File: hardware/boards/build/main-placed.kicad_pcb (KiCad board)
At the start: 4 copper layers, 140 x 84 mm, 151 parts

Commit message: Parts audit complete
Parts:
- removed the REF** at (24.2, 14.8)
- removed the REF** at (40.8, 35.9)
- removed the REF** at (105.9, 14.8)
- removed the REF** at (136.6, 62.5)
- removed the REF** at (111.2, 20.6)
- removed the REF** at (111.0, 14.8)
- removed the REF** at (73.9, 62.6)
- removed the REF** at (91.6, 26.4)
- removed the REF** at (102.9, 30.9)
- removed the REF** at (50.0, 53.3)
- removed the REF** at (18.6, 14.8)
- removed the REF** at (83.8, 62.6)
- removed the REF** at (50.0, 41.0)
- removed the REF** at (111.2, 61.8)
- removed the REF** at (18.6, 9.70)
- removed the REF** at (89.0, 14.8)
- added REF**: SOT-23, BAT54S:SOT-23, F.Cu at (136.6, 25.9)
- added REF**: TSSOP-14, OPA4171AIPWR:TSSOP-14, F.Cu at (107.2, 65.9)
- added REF**: WQFN-16, DAC80508ZRTER:WQFN-16, F.Cu at (49.8, 52.9)
- added REF**: SOD-123, B5819W:SOD-123, F.Cu at (40.6, 35.7)
- added REF**: SOT-23, BAT54S:SOT-23, F.Cu at (136.6, 20.6)
- added REF**: SOD-123, B5819W:SOD-123, F.Cu at (24.1, 14.7)
- added REF**: SOT-23, BAT54S:SOT-23, F.Cu at (110.8, 73.6)
- added REF**: TSSOP-14, OPA4171AIPWR:TSSOP-14, F.Cu at (75.4, 62.6)
- added REF**: TSSOP-14, OPA4171AIPWR:TSSOP-14, F.Cu at (85.8, 62.6)
- added REF**: SOD-123, B5819W:SOD-123, F.Cu at (18.5, 14.7)
- added REF**: TSSOP-14, OPA4171AIPWR:TSSOP-14, F.Cu at (85.5, 73.6)
- added REF**: WQFN-16, DAC80508ZRTER:WQFN-16, F.Cu at (49.8, 40.8)
- added REF**: TSSOP-14, OPA4171AIPWR:TSSOP-14, F.Cu at (107.7, 55.3)
- added REF**: SOT-23, BAT54S:SOT-23, F.Cu at (105.7, 30.6)
- added REF**: SOD-123, B5819W:SOD-123, F.Cu at (18.5, 9.60)
- added REF**: SOT-23, BAT54S:SOT-23, F.Cu at (110.7, 25.6)
- moved C29 83.8 mm to (114.8, 14.7)
- moved C24 83.8 mm to (109.8, 9.60)
- moved R31 79.3 mm to (104.7, 9.60)
- moved R1 79.3 mm to (99.6, 4.53)
- moved R32 74.9 mm to (94.6, 4.53)
- moved C14 74.3 mm to (84.4, 4.53)
- moved C18 72.0 mm to (79.3, 9.60)
- moved C31 70.3 mm to (94.6, 9.60)
- moved C22 69.2 mm to (99.6, 9.60)
- moved R66 69.1 mm to (70.3, 78.6)
- moved C8 67.7 mm to (105.7, 20.5)
- moved C20 67.5 mm to (89.5, 9.60)
- moved C26 66.7 mm to (94.6, 14.7)
- moved C21 66.7 mm to (99.6, 14.7)
- moved C19 66.4 mm to (89.5, 4.53)
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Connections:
- R10 pad 1: 6 -> 9
- R11 pad 1: dac-7-2 -> dac-7-1
- R13 pad 1: 7 -> dac-10
- R16 pad 1: 8 -> 11
- R23 pad 1: dac-7 -> 7
- R37 pad 1: dac-7-1 -> dac-7
- R39 pad 1: dac-7-1 -> dac-7
- R61 pad 1: 5-1 -> 3
- R62 pad 1: 6-1 -> 11-1
- R7 pad 1: 5 -> 8
- R75 pad 2: 3 -> DP
- R9 pad 1: dac-7-2 -> dac-7-1
- REF** pad 1: VBUS -> hv
- REF** pad 2: hv -> VBUS
- REF** pad 4: DM -> DP
- REF** pad 5: 5-1 -> DM
- REF** pad 6: 6-1 -> 6
- REF** pad 7: hv -> VBUS
- REF** pad 2: c_filter-power-hv-4 -> c_vio2-power-hv
- REF** pad 3: c_vio2-power-hv -> c_filter-power-hv-3
- REF** pad 1: BASE -> hv
- REF** pad 2: hv -> BASE-1
- REF** pad 3: COLLECTOR -> COLLECTOR-1
- REF** pad 23: i2c_sda -> 23
- REF** pad 24: i2c_scl -> i2c_sda
- REF** pad 25: 25 -> i2c_scl
- REF** pad 1: BASE-1 -> hv
- REF** pad 2: hv -> BASE
- REF** pad 3: COLLECTOR-1 -> COLLECTOR
- REF** pad 3: 3 -> DP

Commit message: Fix firmware
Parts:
- removed the REF** at (136.6, 25.9)
- removed the REF** at (107.2, 65.9)
- removed the REF** at (49.8, 52.9)
- removed the REF** at (136.6, 57.3)
- removed the REF** at (40.6, 35.7)
- removed the REF** at (136.6, 20.6)
- removed the REF** at (24.1, 14.7)
- removed the REF** at (110.8, 73.6)
- removed the REF** at (75.4, 62.6)
- removed the REF** at (85.8, 62.6)
- removed the REF** at (18.5, 14.7)
- removed the REF** at (85.5, 73.6)
- removed the REF** at (49.8, 40.8)
- removed the REF** at (107.7, 55.3)
- removed the REF** at (105.7, 30.6)
- removed the REF** at (18.5, 9.60)
- removed the REF** at (110.7, 25.6)
- added R76: 27Ω, UNI_ROYAL_0402WGF270JTCE:R0402, F.Cu at (30.5, 55.5)
- added R77: 27Ω, UNI_ROYAL_0402WGF270JTCE:R0402, F.Cu at (30.5, 50.5)
- added REF**: WQFN-16, DAC80508ZRTER:WQFN-16, F.Cu at (70.2, 62.6)
- added REF**: SOT-23, BAT54S:SOT-23, F.Cu at (133.6, 4.50)
- added REF**: SOT-23, BAT54S:SOT-23, F.Cu at (129.5, 78.5)
- added REF**: TSSOP-14, OPA4171AIPWR:TSSOP-14, F.Cu at (88.5, 61.9)
- added REF**: SOT-23, BAT54S:SOT-23, F.Cu at (114.5, 78.5)
- added REF**: TSSOP-14, OPA4171AIPWR:TSSOP-14, F.Cu at (94.5, 68.5)
- added REF**: SOT-23, BAT54S:SOT-23, F.Cu at (128.6, 4.50)
- added REF**: SOT-23, BAT54S:SOT-23, F.Cu at (128.6, 14.5)
- added REF**: SOT-23, BAT54S:SOT-23, F.Cu at (113.5, 4.50)
- added REF**: SOD-123, B5819W:SOD-123, F.Cu at (30.5, 30.5)
- added REF**: WQFN-16, DAC80508ZRTER:WQFN-16, F.Cu at (50.0, 50.5)
- added REF**: TSSOP-14, OPA4171AIPWR:TSSOP-14, F.Cu at (112.2, 67.9)
- added REF**: TSSOP-14, OPA4171AIPWR:TSSOP-14, F.Cu at (92.0, 31.2)
- added REF**: SOD-123, B5819W:SOD-123, F.Cu at (24.0, 14.5)
- added REF**: SOD-123, B5819W:SOD-123, F.Cu at (18.5, 14.5)
- added REF**: TSSOP-14, OPA4171AIPWR:TSSOP-14, F.Cu at (78.6, 62.6)
- added REF**: SOD-123, B5819W:SOD-123, F.Cu at (18.5, 9.50)
- R34, R37, R40, R43: value 6.04kΩ -> 10kΩ; footprint UNI_ROYAL_0402WGF6041TCE:R0402 -> UNI_ROYAL_0603WAF1002T5E:R0603
- R36, R39, R42, R45: value 470Ω -> 6.04kΩ; footprint UNI_ROYAL_0603WAF4700T5E:R0603 -> UNI_ROYAL_0402WGF6041TCE:R0402
- R38, R41, R44, R47: value 10kΩ -> 470Ω; footprint UNI_ROYAL_0603WAF1002T5E:R0603 -> UNI_ROYAL_0603WAF4700T5E:R0603
- R46: value 200Ω -> 10kΩ; footprint UNI_ROYAL_0603WAF2000T5E:R0603 -> UNI_ROYAL_0603WAF1002T5E:R0603
- R48: value 10kΩ -> 200Ω; footprint UNI_ROYAL_0603WAF1002T5E:R0603 -> UNI_ROYAL_0603WAF2000T5E:R0603
- R50: value 22kΩ -> 10kΩ; footprint UNI_ROYAL_0603WAF2202T5E:R0603 -> UNI_ROYAL_0603WAF1002T5E:R0603
- R61: value 5.1kΩ -> 10kΩ; footprint UNI_ROYAL_0402WGF5101TCE:R0402 -> UNI_ROYAL_0603WAF1002T5E:R0603
- R62: value 5.1kΩ -> 22kΩ; footprint UNI_ROYAL_0402WGF5101TCE:R0402 -> UNI_ROYAL_0603WAF2202T5E:R0603
- R63, R64: value 1kΩ -> 5.1kΩ; footprint UNI_ROYAL_0603WAF1001T5E:R0603 -> UNI_ROYAL_0402WGF5101TCE:R0402
- R65, R66, R73: value 10kΩ -> 1kΩ; footprint UNI_ROYAL_0603WAF1002T5E:R0603 -> UNI_ROYAL_0603WAF1001T5E:R0603
- R71, R72: value 1kΩ -> 10kΩ; footprint UNI_ROYAL_0603WAF1001T5E:R0603 -> UNI_ROYAL_0603WAF1002T5E:R0603
- R74: value 27Ω -> 1kΩ; footprint UNI_ROYAL_0402WGF270JTCE:R0402 -> UNI_ROYAL_0603WAF1001T5E:R0603
- R75: value 27Ω -> 10kΩ; footprint UNI_ROYAL_0402WGF270JTCE:R0402 -> UNI_ROYAL_0603WAF1002T5E:R0603
- moved R64 132.8 mm to (4.58, 37.9)
- moved R62 125.1 mm to (124.5, 73.5)
- moved R74 107.1 mm to (136.6, 36.3)
- moved R55 101.5 mm to (53.5, 9.50)
- moved R50 96.1 mm to (40.5, 35.5)
- moved R63 95.9 mm to (9.75, 37.9)
- moved R49 93.1 mm to (35.5, 40.5)
- moved C29 92.6 mm to (39.5, 68.5)
- moved C24 91.3 mm to (44.5, 73.5)
- moved R59 86.7 mm to (63.5, 4.50)
- moved R57 84.2 mm to (49.5, 73.5)
- moved C47 82.8 mm to (54.5, 73.5)
- moved R66 81.6 mm to (136.6, 31.1)
- moved R32 81.5 mm to (40.5, 65.5)
- moved R31 81.4 mm to (45.5, 65.5)
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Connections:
- R34 pad 1: dac-1 -> c_vio2-power-hv
- R34 pad 2: dac-IN1_N-1 -> SDO
- R35 pad 1: dac-IN1_N-1 -> c_vio2-power-hv
- R35 pad 2: hv -> dac-SDO
- R36 pad 2: vel1 -> dac-IN1_N-1
- R37 pad 1: dac-7 -> dac-IN1_N-1
- R37 pad 2: dac-IN2_N-1 -> hv
- R38 pad 1: dac-IN2_N-1 -> dac-1
- R38 pad 2: hv -> vel1
- R39 pad 2: vel2 -> dac-IN2_N-1
- R40 pad 1: dac-8-1 -> dac-IN2_N-1
- R40 pad 2: dac-IN3_N-1 -> hv
- R41 pad 1: dac-IN3_N-1 -> dac-7
- R41 pad 2: hv -> vel2
- R42 pad 2: vel3 -> dac-IN3_N-1
- R43 pad 1: dac-14 -> dac-IN3_N-1
- R43 pad 2: dac-IN4_N-1 -> hv
- R44 pad 1: dac-IN4_N-1 -> dac-8-1
- R44 pad 2: hv -> vel3
- R45 pad 2: vel4 -> dac-IN4_N-1
- R46 pad 1: c_3v3_bulk-power-hv -> dac-IN4_N-1
- R46 pad 2: c_aref-power-hv -> hv
- R47 pad 1: c_3v3_bulk-power-hv -> dac-14
- R47 pad 2: BS -> vel4
- R48 pad 2: RUN -> c_aref-power-hv
- R49 pad 1: c_filter-power-hv -> c_3v3_bulk-power-hv
- R49 pad 2: hv -> BS
- R50 pad 1: clk_in -> c_3v3_bulk-power-hv
- R50 pad 2: c_filter-power-hv -> RUN
- R51 pad 1: c_filter-power-hv-1 -> c_filter-power-hv
- R52 pad 1: cv_a -> clk_in
- R52 pad 2: c_filter-power-hv-1 -> c_filter-power-hv
- R53 pad 1: c_filter-power-hv-2 -> c_filter-power-hv-1
- R54 pad 1: cv_b -> cv_a
- R54 pad 2: c_filter-power-hv-2 -> c_filter-power-hv-1
- R55 pad 1: c_filter-power-hv-3 -> c_filter-power-hv-2
- R56 pad 1: cv_c -> cv_b
- R56 pad 2: c_filter-power-hv-3 -> c_filter-power-hv-2
- R57 pad 1: c_filter-power-hv-4 -> c_filter-power-hv-3
- R58 pad 1: cv_d -> cv_c
- R58 pad 2: c_filter-power-hv-4 -> c_filter-power-hv-3
- R59 pad 1: c_filter-power-hv-5 -> c_filter-power-hv-4
- R60 pad 1: input -> cv_d
- R60 pad 2: c_filter-power-hv-5 -> c_filter-power-hv-4
- R61 pad 1: 3 -> c_filter-power-hv-5
- R62 pad 1: 11-1 -> input
- R62 pad 2: hv -> c_filter-power-hv-5
- R63 pad 1: clk_out -> 3
- R63 pad 2: BASE -> hv
- R64 pad 1: c_5v_hf-power-hv -> 11-1
- R64 pad 2: COLLECTOR -> hv
- R65 pad 1: c_vio2-power-hv -> clk_out
- R65 pad 2: c_enc_a_a-power-hv -> BASE
- R66 pad 1: c_vio2-power-hv -> c_5v_hf-power-hv
- R66 pad 2: c_enc_a_b-power-hv -> COLLECTOR
- R67 pad 2: c_enc_a_sw-power-hv -> c_enc_a_a-power-hv
- R68 pad 2: c_enc_b_a-power-hv -> c_enc_a_b-power-hv
- R69 pad 2: c_enc_b_b-power-hv -> c_enc_a_sw-power-hv
- R70 pad 2: c_enc_b_sw-power-hv -> c_enc_b_a-power-hv
- R71 pad 1: rst_out -> c_vio2-power-hv
- R71 pad 2: BASE-1 -> c_enc_b_b-power-hv
- R72 pad 1: c_5v_hf-power-hv -> c_vio2-power-hv
- R72 pad 2: COLLECTOR-1 -> c_enc_b_sw-power-hv
- R73 pad 1: c_vio2-power-hv -> rst_out
- R73 pad 2: sd_cd -> BASE-1
- R74 pad 1: usb_dm -> c_5v_hf-power-hv
- R74 pad 2: DM -> COLLECTOR-1
- R75 pad 1: usb_dp -> c_vio2-power-hv
- R75 pad 2: DP -> sd_cd

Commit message: Fix visuals
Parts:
- removed the REF** at (133.6, 4.50)
- removed the REF** at (129.5, 78.5)
- removed the REF** at (88.5, 61.9)
- removed the REF** at (114.5, 78.5)
- removed the REF** at (94.5, 68.5)
- removed the REF** at (128.6, 4.50)
- removed the REF** at (128.6, 14.5)
- removed the REF** at (113.5, 4.50)
- removed the REF** at (92.0, 31.2)
- removed the REF** at (78.6, 62.6)
- added REF**: TSSOP-14, OPA4171AIPWR:TSSOP-14, F.Cu at (85.8, 62.6)
- added REF**: SOT-23, BAT54S:SOT-23, F.Cu at (105.7, 20.5)
- added REF**: TSSOP-14, OPA4171AIPWR:TSSOP-14, F.Cu at (95.6, 30.6)
- added REF**: SOT-23, BAT54S:SOT-23, F.Cu at (136.6, 25.9)
- added REF**: TSSOP-14, OPA4171AIPWR:TSSOP-14, F.Cu at (95.6, 65.9)
- added REF**: SOT-23, BAT54S:SOT-23, F.Cu at (136.6, 57.3)
- added REF**: TSSOP-14, OPA4171AIPWR:TSSOP-14, F.Cu at (89.5, 73.5)
- added REF**: SOT-23, BAT54S:SOT-23, F.Cu at (110.7, 20.5)
- added REF**: SOT-23, BAT54S:SOT-23, F.Cu at (110.7, 25.6)
- added REF**: SOT-23, BAT54S:SOT-23, F.Cu at (136.6, 62.5)
- moved R53 103.2 mm to (129.5, 73.5)
- moved R57 102.7 mm to (133.6, 14.5)
- moved R51 102.7 mm to (134.5, 78.5)
- moved C47 97.7 mm to (136.6, 20.6)
- moved R61 87.6 mm to (103.5, 9.50)
- moved R30 83.7 mm to (93.5, 4.50)
- moved R33 80.7 mm to (98.5, 4.50)
- moved C17 78.8 mm to (119.5, 73.5)
- moved C10 78.4 mm to (114.5, 78.5)
- moved C19 76.9 mm to (119.5, 78.5)
- moved C44 75.6 mm to (134.5, 73.5)
- moved C16 75.0 mm to (129.5, 68.5)
- moved R1 75.0 mm to (88.5, 4.50)
- moved C24 75.0 mm to (83.5, 9.50)
- moved C20 74.9 mm to (93.5, 9.50)
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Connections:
- REF** pad 1: c_5v_hf-power-hv -> power-1
- REF** pad 2: anode -> lv
- REF** pad 1: power-1 -> c_5v_hf-power-hv
- REF** pad 2: lv -> anode
- REF** pad 2: BASE -> BASE-1
- REF** pad 3: COLLECTOR -> COLLECTOR-1
- REF** pad 13: 13 -> (no net)
- REF** pad 14: power.header-14 -> (no net)
- REF** pad 15: 15 -> (no net)
- REF** pad 16: 16 -> (no net)
- REF** pad 2: BASE-1 -> BASE
- REF** pad 3: COLLECTOR-1 -> COLLECTOR

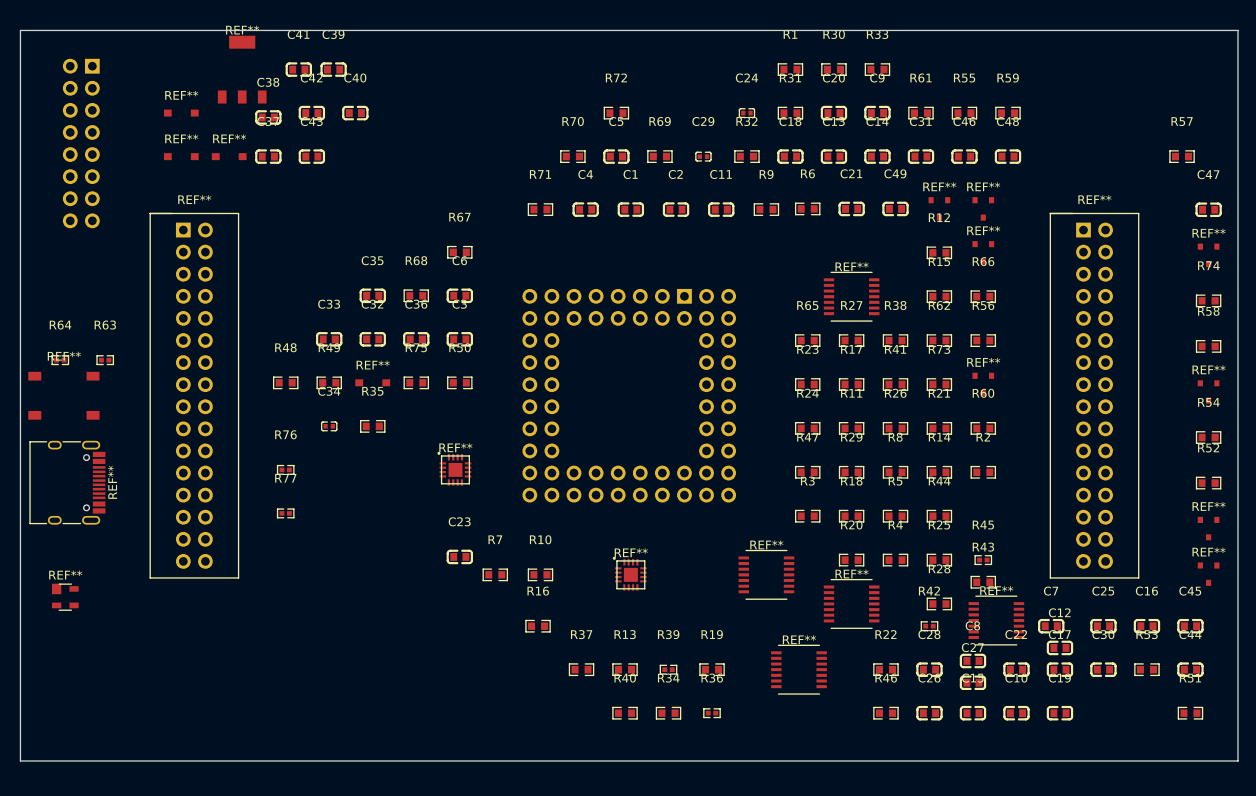
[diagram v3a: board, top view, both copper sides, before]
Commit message: production check command and fixes coming out of that
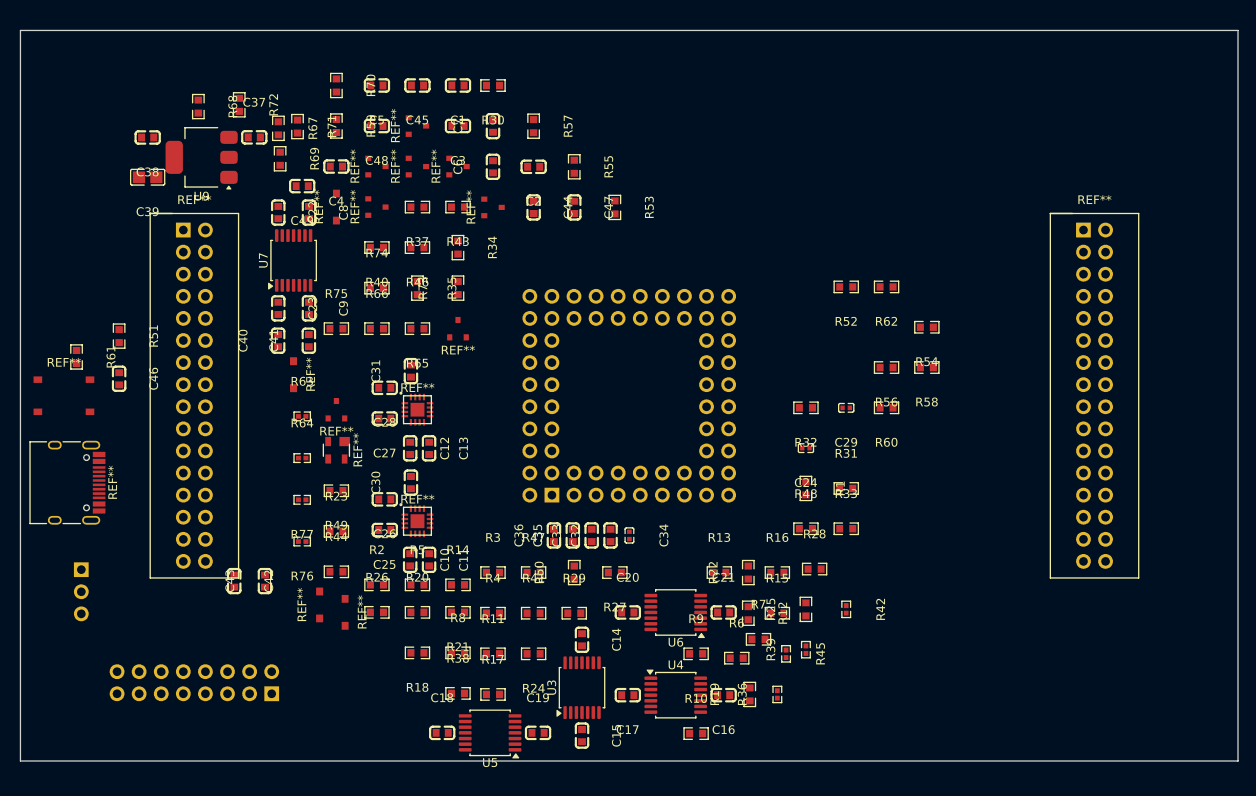
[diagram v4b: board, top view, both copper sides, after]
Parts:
- removed the REF** at (85.8, 62.6)
- removed the REF** at (18.5, 14.5)
- removed the REF** at (40.5, 40.5)
- removed the REF** at (105.7, 20.5)
- removed the REF** at (95.6, 30.6)
- removed the REF** at (5.00, 42.0)
- removed the REF** at (136.6, 25.9)
- removed the REF** at (95.6, 65.9)
- removed the REF** at (136.6, 57.3)
- removed the REF** at (89.5, 73.5)
- removed the REF** at (24.0, 14.5)
- removed the REF** at (110.7, 20.5)
- removed the REF** at (18.5, 9.50)
- removed the REF** at (25.5, 4.50)
- removed the REF** at (136.6, 41.6)
- removed the REF** at (112.2, 67.9)
- removed the REF** at (70.2, 62.6)
- removed the REF** at (110.7, 25.6)
- removed the REF** at (50.0, 50.5)
- removed the REF** at (110.7, 40.7)
- removed the REF** at (136.6, 62.5)
- added REF**: SOT-23, BAT54S:SOT-23, F.Cu at (50.3, 15.6)
- added REF**: SOT-23, BAT54S:SOT-23, F.Cu at (41.0, 20.3)
- added REF**: SOD-123, B5819W:SOD-123, F.Cu at (34.4, 66.1)
- added REF**: SOT-23, 2N3904:SOT-23, F.Cu at (36.3, 43.6)
- added REF**: SOD-123, B5819W:SOD-123, F.Cu at (36.3, 20.3)
- added REF**: SOD-123, B5819W:SOD-123, F.Cu at (31.4, 39.6)
- added REF**: SOT-23, BAT54S:SOT-23, F.Cu at (45.6, 15.6)
- added REF**: SW_SPST_TS1187A, TactileSwitch:SW_SPST_TS1187A, F.Cu at (5.00, 42.0)
- added REF**: SOD-123, B5819W:SOD-123, F.Cu at (37.3, 66.9)
- added REF**: PinHeader1x3, PinHeader1x3:PinHeader1x3, B.Cu at (7.00, 62.0)
- added REF**: WQFN-16, DAC80508ZRTER:WQFN-16, F.Cu at (45.6, 43.6)
- added REF**: SOT-23, BAT54S:SOT-23, F.Cu at (54.3, 20.3)
- added REF**: SOT-23, BAT54S:SOT-23, F.Cu at (41.0, 15.6)
- added REF**: SOT-23, 2N3904:SOT-23, F.Cu at (50.3, 34.3)
- added REF**: SOT-23, BAT54S:SOT-23, F.Cu at (45.6, 11.0)
- added REF**: WQFN-16, DAC80508ZRTER:WQFN-16, F.Cu at (45.6, 56.4)
- added U3: , OPA4171AIPWR:TSSOP-14, F.Cu at (64.6, 75.6)
- added U4: , OPA4171AIPWR:TSSOP-14, F.Cu at (75.3, 76.4)
- added U5: , OPA4171AIPWR:TSSOP-14, F.Cu at (54.0, 80.8)
- added U6: , OPA4171AIPWR:TSSOP-14, F.Cu at (75.3, 66.9)
- added U7: , OPA4171AIPWR:TSSOP-14, F.Cu at (31.4, 26.4)
- added U9: , AMS1117-3.3:SOT-223, F.Cu at (20.8, 14.6)
- C39: value 10µF -> 47µF; footprint Samsung_Electro_Mechanics_CL10A106KP8NNNC:C0603 -> Samsung_Electro_Mechanics_CL21A476MQYNNNE:C0805
- moved R51 130.6 mm to (11.3, 35.1), turned to -90 degrees
- moved C45 108.5 mm to (45.6, 6.33), turned to 180 degrees
- moved R61 101.1 mm to (6.45, 37.5), turned to -90 degrees
- moved C46 100.5 mm to (11.3, 40.0), turned to -90 degrees
- moved C22 99.8 mm to (29.6, 20.9), turned to -90 degrees
- moved R74 95.6 mm to (41.0, 29.6)
- moved C44 92.4 mm to (59.0, 20.3), turned to -90 degrees
- moved C8 92.1 mm to (33.2, 20.9), turned to -90 degrees
- moved C7 86.2 mm to (54.3, 11.0), turned to 90 degrees
- moved C25 83.4 mm to (41.9, 57.4), turned to 180 degrees
- moved C30 82.5 mm to (44.9, 52.0), turned to 90 degrees
- moved R53 81.0 mm to (68.3, 20.3), turned to -90 degrees
- moved C12 78.2 mm to (44.8, 48.0), turned to -90 degrees
- moved C18 77.4 mm to (48.5, 80.8)
- moved R59 77.2 mm to (36.3, 11.0), turned to -90 degrees
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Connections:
- R50 pad 2: RUN -> P_RUN

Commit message: Increase cutouts for encoders & jacks
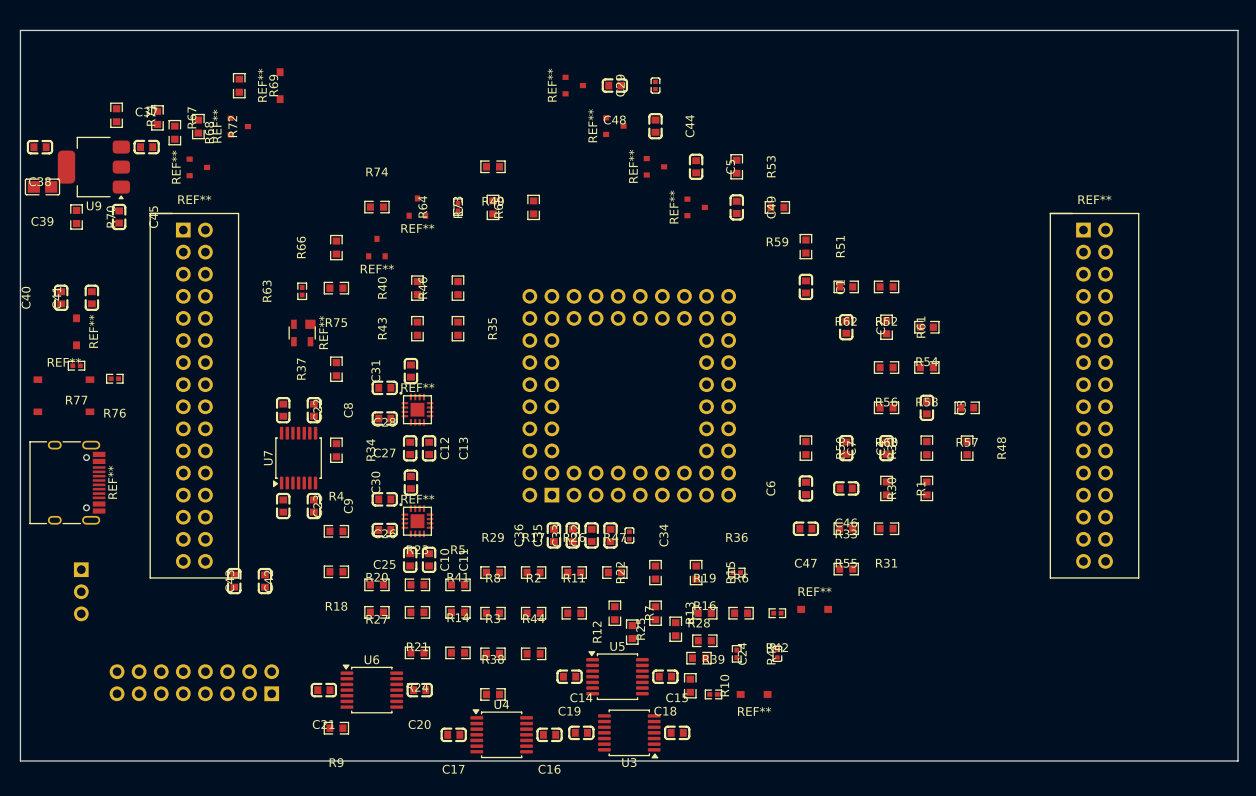
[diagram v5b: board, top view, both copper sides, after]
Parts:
- removed the REF** at (50.3, 15.6)
- removed the REF** at (41.0, 20.3)
- removed the REF** at (34.4, 66.1)
- removed the REF** at (36.3, 43.6)
- removed the REF** at (36.3, 20.3)
- removed the REF** at (31.4, 39.6)
- removed the REF** at (45.6, 15.6)
- removed the REF** at (37.3, 66.9)
- removed the REF** at (54.3, 20.3)
- removed the REF** at (41.0, 15.6)
- removed the REF** at (50.3, 34.3)
- removed the REF** at (45.6, 11.0)
- added REF**: SOD-123, B5819W:SOD-123, F.Cu at (91.3, 66.6)
- added REF**: SOD-123, B5819W:SOD-123, F.Cu at (6.45, 34.6)
- added REF**: SOD-123, B5819W:SOD-123, F.Cu at (84.4, 76.3)
- added REF**: SOT-23, BAT54S:SOT-23, F.Cu at (68.3, 11.0)
- added REF**: SOT-23, BAT54S:SOT-23, F.Cu at (63.7, 6.34)
- added REF**: SOD-123, B5819W:SOD-123, F.Cu at (29.9, 6.35)
- added REF**: SOT-23, 2N3904:SOT-23, F.Cu at (41.0, 25.0)
- added REF**: SOT-23, BAT54S:SOT-23, F.Cu at (20.5, 15.8)
- added REF**: SOT-23, BAT54S:SOT-23, F.Cu at (73.0, 15.7)
- added REF**: SOT-23, 2N3904:SOT-23, F.Cu at (45.6, 20.3)
- added REF**: SOT-23, BAT54S:SOT-23, F.Cu at (77.7, 20.3)
- added REF**: SOT-23, BAT54S:SOT-23, F.Cu at (25.2, 11.1)
- moved R61 93.2 mm to (99.6, 34.1)
- moved C46 84.5 mm to (95.0, 52.7), turned to 180 degrees
- moved R51 79.6 mm to (90.3, 24.9)
- moved R30 68.1 mm to (104.2, 52.7), turned to 90 degrees
- moved C4 67.0 mm to (95.0, 48.0), turned to -90 degrees
- moved C3 62.9 mm to (104.2, 43.4), turned to -90 degrees
- moved R57 59.4 mm to (108.9, 43.4), turned to 180 degrees
- moved C7 58.5 mm to (99.6, 48.0)
- moved R55 52.1 mm to (95.0, 57.3), turned to 180 degrees
- moved C6 51.6 mm to (90.3, 52.7)
- moved R59 51.6 mm to (87.0, 20.3), turned to 180 degrees
- moved C49 50.0 mm to (82.4, 20.3), turned to -90 degrees
- moved C21 46.8 mm to (34.9, 75.8), turned to 180 degrees
- moved C1 46.2 mm to (90.3, 29.5), turned to -90 degrees
- moved C47 45.6 mm to (90.3, 57.3), turned to 180 degrees
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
